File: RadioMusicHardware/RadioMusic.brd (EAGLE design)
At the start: 106 x 49 mm, 63 parts, among them IC2 7805L, IC3 TL072P, IC4 TL072P

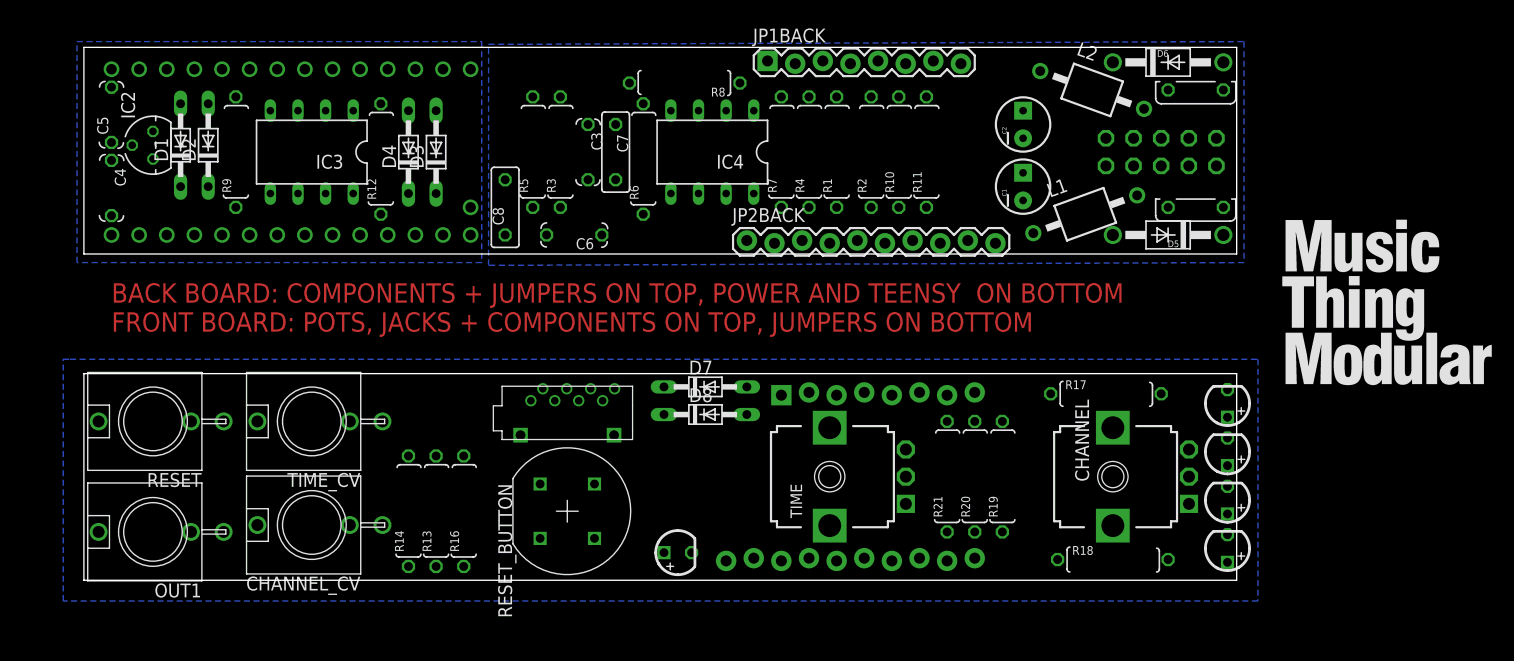
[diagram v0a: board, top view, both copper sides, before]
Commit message: First autorouted board
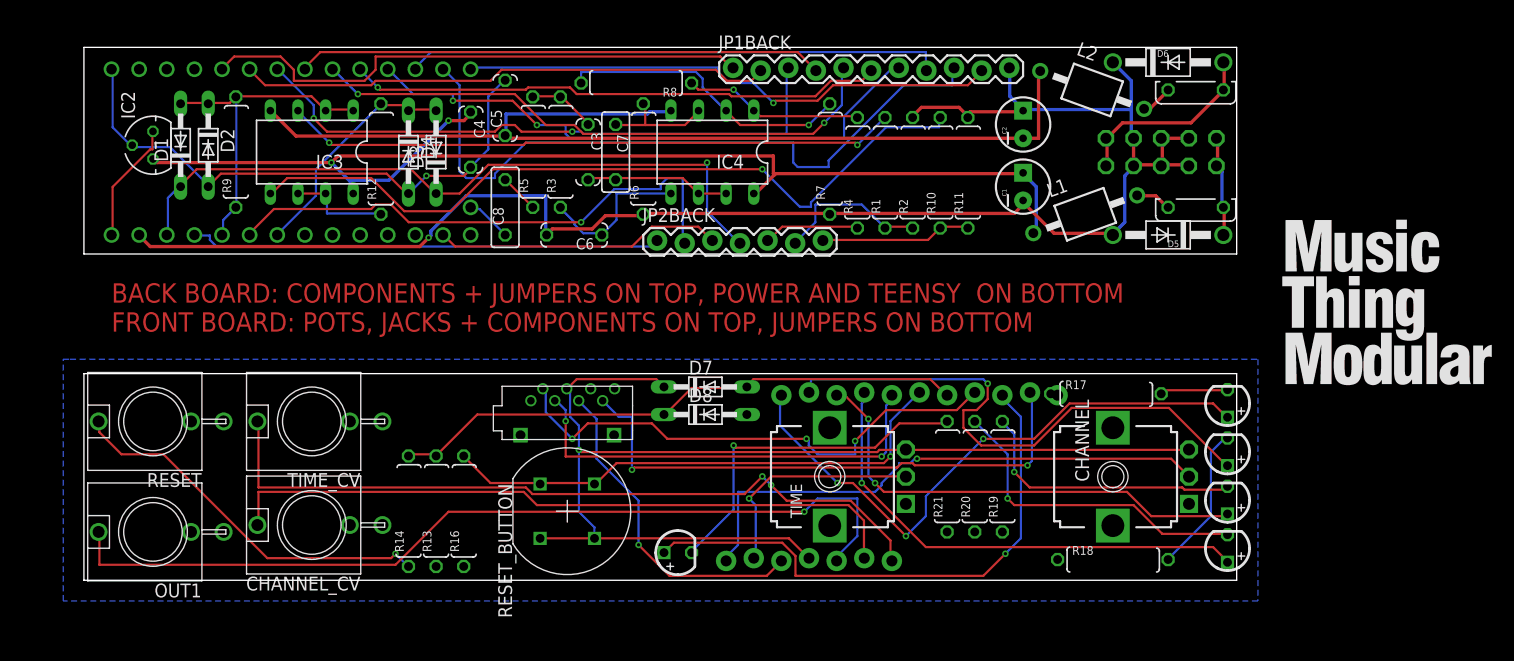
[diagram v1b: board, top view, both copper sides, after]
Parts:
- JP1BACK, JP1FRONT: value (none) -> M11LOCK; device SparkFun-Connectors:1X08_LOCK -> SparkFun-Connectors:1X11_LOCK
- JP2BACK, JP2FRONT: value M10LOCK -> (none); device SparkFun-Connectors:1X10_LOCK -> SparkFun-Connectors:1X07_LOCK
- moved C5 36.2 mm to (38.7, 43.4)
- moved C4 33.3 mm to (35.6, 40.5)
- moved JP2BACK 8.26 mm to (52.7, 31.1)
- moved R4 4.84 mm to (71.1, 37.5)
- moved R1 4.84 mm to (73.7, 37.5)
- moved R7 4.49 mm to (68.6, 38.7)
- moved R8 4.45 mm to (50.8, 45.7)
- moved R11 4.26 mm to (81.3, 37.5)
- moved R2 4.26 mm to (76.2, 37.5)
- moved R10 4.26 mm to (78.7, 37.5)
- moved JP1BACK 3.24 mm to (59.7, 47.0)
- turned D2 to 270 degrees
- turned D4 to 270 degrees
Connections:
- net +3.3V: now also JP2BACK.4; no longer JP2BACK.1
- net +3.3V_F: now also JP2FRONT.4; no longer JP2FRONT.1
- net CHANNEL_CV: now also JP2BACK.6; no longer JP2BACK.8
- net CHANNEL_CV_F: now also JP2FRONT.6; no longer JP2FRONT.8
- net CHANNEL_POT: now also JP2BACK.1; no longer JP2BACK.7
- net CHANNEL_POT_F: now also JP2FRONT.1; no longer JP2FRONT.7
- net GND: now also JP1BACK.11; no longer JP1BACK.8
- net GND_F: now also JP1FRONT.11; no longer JP1FRONT.8
- net LED1: now also JP1BACK.1; no longer JP1BACK.6
- net LED1_F: now also JP1FRONT.1; no longer JP1FRONT.6
- net LED2: now also JP1BACK.2; no longer JP1BACK.5
- net LED2_F: now also JP1FRONT.2; no longer JP1FRONT.5
- net LED3: now also JP1BACK.3; no longer JP1BACK.4
- net LED3_F: now also JP1FRONT.3; no longer JP1FRONT.4
- net LED4: now also JP1BACK.4; no longer JP1BACK.3
- net LED4_F: now also JP1FRONT.4; no longer JP1FRONT.3
- net LED_RESET: now also JP1BACK.9; no longer JP1BACK.2
- net LED_RESET_F: now also JP1FRONT.9; no longer JP1FRONT.2
- net MISO: now also JP1BACK.10; no longer JP2BACK.4
- net MISO_F: now also JP1FRONT.10; no longer JP2FRONT.4
- net MOSI: now also JP1BACK.5; no longer JP2BACK.3
- net MOSI_F: now also JP1FRONT.5; no longer JP2FRONT.3
- net RESET_CV: now also JP1BACK.7; no longer JP2BACK.10
- net RESET_CV_F: now also JP1FRONT.7; no longer JP2FRONT.10
- net RESET_SW: now also JP1BACK.6; no longer JP1BACK.1
- net RESET_SW_F: now also JP1FRONT.6; no longer JP1FRONT.1
- net SCLK: now also JP2BACK.3; no longer JP2BACK.2
- net SCLK_F: now also JP2FRONT.3; no longer JP2FRONT.2
- net SS: now also JP1BACK.8; no longer JP1BACK.7
- net SS_F: now also JP1FRONT.8; no longer JP1FRONT.7
- net TIME_CV: now also JP2BACK.7; no longer JP2BACK.9
- net TIME_CV_F: now also JP2FRONT.7; no longer JP2FRONT.9
- net TIME_POT: now also JP2BACK.2; no longer JP2BACK.6
- net TIME_POT_F: now also JP2FRONT.2; no longer JP2FRONT.6
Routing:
- net GND: track 0.00 -> 152.5 mm, vias 0 -> 1
- net +12V: track 0.00 -> 108.5 mm, vias 0 -> 2
- net +3.3V_F: track 0.00 -> 106.2 mm, vias 0 -> 1
- net -12V: track 0.00 -> 95.3 mm
- net AUDIO_OUT_F: track 0.00 -> 81.8 mm, vias 0 -> 1
- net N$12: track 0.00 -> 70.6 mm, vias 0 -> 1
- net TIME_CV_F: track 0.00 -> 69.5 mm, vias 0 -> 2
- net +3.3V: track 0.00 -> 65.0 mm, vias 0 -> 1
- net LED_RESET: track 0.00 -> 64.3 mm
- net CHANNEL_CV_F: track 0.00 -> 63.4 mm
- net LED3: track 0.00 -> 56.6 mm, vias 0 -> 2
- net N$3: track 0.00 -> 56.5 mm, vias 0 -> 2
- net LED1_F: track 0.00 -> 54.8 mm, vias 0 -> 3
- net RESET_CV: track 0.00 -> 54.3 mm, vias 0 -> 2
- net MOSI: track 0.00 -> 53.9 mm, vias 0 -> 2
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- removed copper zone on layer 16, net DGND
- removed copper zone on layer 16, net GND

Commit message: Add output level trim
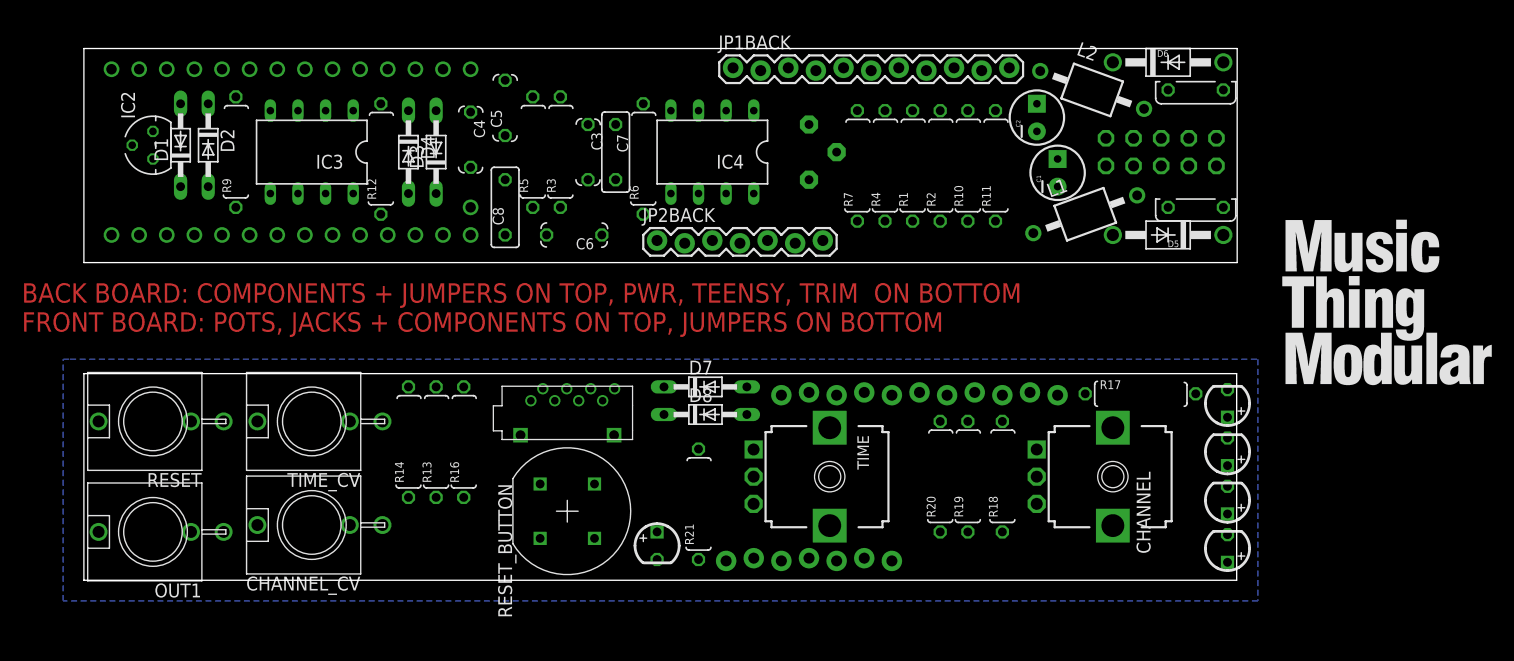
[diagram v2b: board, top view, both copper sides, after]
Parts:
- removed R8: 3.3K, TomW:0207/10
- added R15: (no value), bourns:3362P
- moved R21 23.0 mm to (56.5, 6.99)
- moved R18 12.7 mm to (84.5, 9.53), turned to 90 degrees
- moved R13 6.35 mm to (32.4, 12.7)
- moved R14 6.35 mm to (29.8, 12.7)
- moved R16 6.35 mm to (34.9, 12.7)
- moved C1 3.42 mm to (89.5, 37.5)
- moved R20 3.18 mm to (78.7, 9.53)
- moved R17 3.17 mm to (97.2, 17.1)
- moved R19 3.17 mm to (81.3, 9.53)
- moved R1 2.62 mm to (76.2, 38.1)
- moved R10 2.62 mm to (81.3, 38.1)
- moved R7 2.62 mm to (71.1, 38.1)
- moved R11 2.62 mm to (83.8, 38.1)
- moved R2 2.62 mm to (78.7, 38.1)
- moved R4 2.62 mm to (73.7, 38.1)
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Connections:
- net GND_F: now also R16.2, R20.2, R21.2; no longer R16.1, R20.1, R21.1
- net N$21: now also R20.1; no longer R20.2
- net N$25: now also R21.1; no longer R21.2
- net N$7: now also R15.1; no longer R8.2
- net N$8: now also R15.2, R15.3; no longer R8.1
- net RESET_SW_F: now also R16.1; no longer R16.2
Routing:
- net GND: track 152.5 -> 0.00 mm, vias 1 -> 0
- net +12V: track 108.5 -> 0.00 mm, vias 2 -> 0
- net +3.3V_F: track 106.2 -> 0.00 mm, vias 1 -> 0
- net -12V: track 95.3 -> 0.00 mm
- net AUDIO_OUT_F: track 81.8 -> 0.00 mm, vias 1 -> 0
- net N$12: track 70.6 -> 0.00 mm, vias 1 -> 0
- net TIME_CV_F: track 69.5 -> 0.00 mm, vias 2 -> 0
- net +3.3V: track 65.0 -> 0.00 mm, vias 1 -> 0
- net LED_RESET: track 64.3 -> 0.00 mm
- net CHANNEL_CV_F: track 63.4 -> 0.00 mm
- net LED3: track 56.6 -> 0.00 mm, vias 2 -> 0
- net N$3: track 56.5 -> 0.00 mm, vias 2 -> 0
- net LED1_F: track 54.8 -> 0.00 mm, vias 3 -> 0
- net RESET_CV: track 54.3 -> 0.00 mm, vias 2 -> 0
- net MOSI: track 53.9 -> 0.00 mm, vias 2 -> 0
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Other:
- board size 106 x 49 mm -> 106 x 48.9 mm
- board text added: "BACK BOARD: COMPONENTS + JUMPERS ON TOP, PWR, TEENSY, TRIM ON BOTTOM FRONT BOARD: POTS, JACKS + COMPONENTS ON TOP, JUMPERS ON BOTTOM"
- board text removed: "BACK BOARD: COMPONENTS + JUMPERS ON TOP, POWER AND TEENSY ON BOTTOM FRONT BOARD: POTS, JACKS + COMPONENTS ON TOP, JUMPERS ON BOTTOM"

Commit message: Add reset LED
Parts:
- renumbered R15 to VOLUME

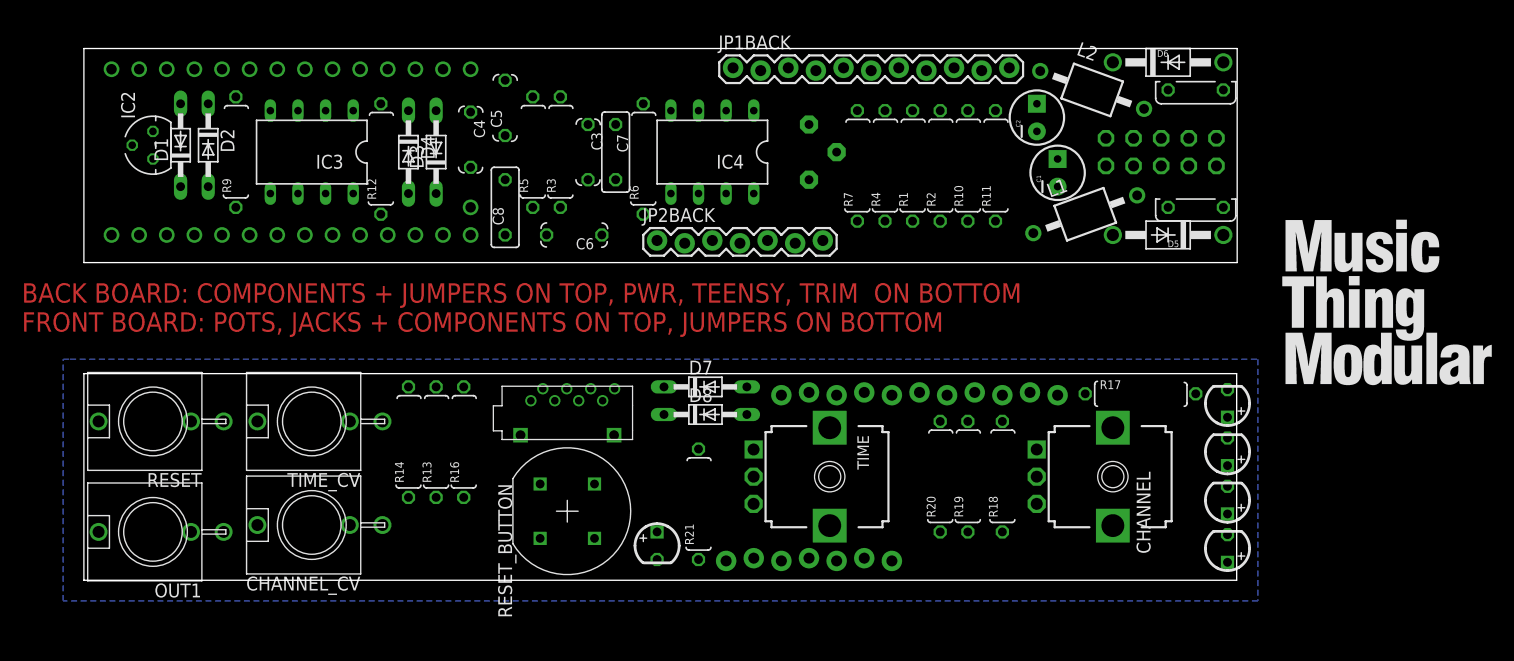
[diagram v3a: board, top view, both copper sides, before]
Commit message: Renumber Parts
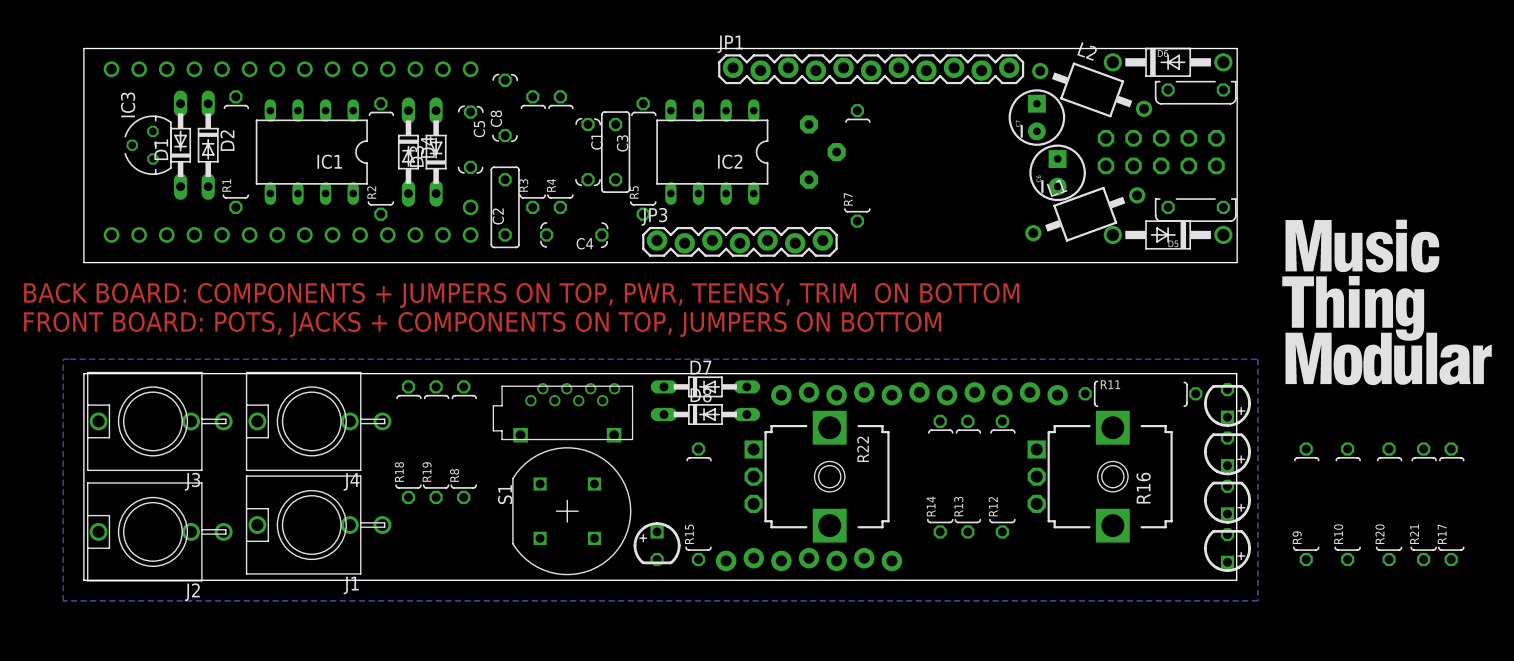
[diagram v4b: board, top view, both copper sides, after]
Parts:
- removed CHANNEL: 50k, TomW:EVUF
- removed IC4: TL072P, TomW:DIL08
- removed VOLUME: (no value), bourns:3362P
- added IC1: TL072P, TomW:DIL08
- added R15: 1k, TomW:0207/10
- added R8: 10k, TomW:0207/10
- C1: value 10uf -> 1n; device SparkFun-Passives:CPOL-RADIAL-10UF-25V -> TomW:C050-024X044
- C2: value 10uf -> 100n; device SparkFun-Passives:CPOL-RADIAL-10UF-25V -> TomW:C050-025X075
- C3: value 1n -> 100n; device TomW:C050-024X044 -> TomW:C050-025X075
- C4: value 100n -> 1n
- C6: value 1n -> 10uf; device TomW:C050-024X044 -> SparkFun-Passives:CPOL-RADIAL-10UF-25V
- C7: value 100n -> 10uf; device TomW:C050-025X075 -> SparkFun-Passives:CPOL-RADIAL-10UF-25V
- C8: device TomW:C050-025X075 -> TomW:C050-024X044
- IC2: value 7805L -> TL072P; device gm-regulators:TO92 -> TomW:DIL08
- IC3: value TL072P -> 7805L; device TomW:DIL08 -> gm-regulators:TO92
- R1: value 100k -> 47R
- R10: value 100k -> 200k
- R11: value 200k -> 1k
- R12: value 47R -> 1k
- R13: value 100k -> 1k
- R14: value 220R -> 1k
- R16: value 10k -> 50k; device TomW:0207/10 -> TomW:EVUF
- R17, R18: value 1k -> 220R
- R19, R20: value 1k -> 100k
- R2: value 200k -> 47R
- R21: value 1k -> 200k
- R4: value 220R -> 8.2k
- R5: value 8.2k -> 330K
- R6: value 330K -> (none); device TomW:0207/10 -> bourns:3362P
- R9: value 47R -> 100k
- moved R9 103.6 mm to (112.4, 6.99)
- moved R21 66.7 mm to (123.2, 6.99)
- moved R12 64.2 mm to (84.5, 9.53)
- moved R1 62.2 mm to (14.0, 39.4)
- moved R16 59.8 mm to (94.6, 9.53), turned to 270 degrees
- moved R18 54.7 mm to (29.8, 12.7)
- moved IC2 51.4 mm to (57.8, 39.4), turned to 180 degrees
- moved R2 51.4 mm to (27.3, 38.7)
- moved C2 49.6 mm to (38.7, 34.3)
- moved R13 49.0 mm to (81.3, 9.53)
- moved R19 49.0 mm to (32.4, 12.7)
- moved R14 49.0 mm to (78.7, 9.53)
- moved R10 46.8 mm to (116.2, 6.99)
- moved C6 44.8 mm to (89.5, 37.5), turned to 90 degrees
- moved C1 43.2 mm to (46.4, 39.4), turned to 270 degrees
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- renumbered 1 to F1, CHANNEL_CV to J1, FUSE to F2, JP1BACK to JP1, JP1FRONT to JP2, JP2BACK to JP3, JP2FRONT to JP4, OUT1 to J2, RESET to J3, RESET_BUTTON to S1, RESET_LED to LED5, TIME to R22, TIME_CV to J4, U$1 to U1, U$3 to X1
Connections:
- removed net N$12: IC3.5, R10.2
- removed net N$8: IC4.1, R4.2, VOLUME.2, VOLUME.3
- new net N$9: J1.P$1, R10.1, R9.1
- new net TEMP: J4.P$1, R20.1, R21.1
- net +12V: now also C5.1, C6.1, IC1.8, IC2.8, IC3.1; no longer C1.1, C4.1, IC2.1, IC3.8, IC4.8
- net +3.3V_F: now also R16.3; no longer CHANNEL.3
- net +5V: now also IC3.3; no longer IC2.3
- net -12V: now also C7.2, C8.1, IC1.4, IC2.4; no longer C2.2, C5.1, IC3.4, IC4.4
- net AUDIO_OUT: now also IC2.1, R6.2, R6.3; no longer R4.1
- net AUDIO_OUT_F: now also R17.2; no longer J2.P$1
- net CHANNEL_CV: now also IC1.3; no longer R1.1, R2.1
- net CHANNEL_CV_F: now also R9.2; no longer J1.P$1
- net CHANNEL_POT_F: now also R16.2; no longer CHANNEL.2
- net DAC: now also C2.1; no longer C8.1
- net DGND: now also C8.2, IC3.2; no longer C4.2, IC2.2
- net GND: now also C4.2, C7.1, R10.2, R21.2, R5.1; no longer C1.2, C2.1, R11.2, R2.2, R6.1
- net GND_F: now also R11.1, R12.1, R14.2, R15.2, R16.1, R8.2; no longer CHANNEL.1, R16.2, R17.1, R18.1, R20.2, R21.2
- net N$1: now also IC1.6, IC1.7, R2.1; no longer IC3.6, IC3.7, R12.1
- net N$10: now also C2.2, R3.1; no longer C8.2, R5.1
- net N$14: now also R18.1; no longer R14.1
- net N$18: now also R11.2; no longer R17.2
- net N$19: now also R12.2; no longer R18.2
- net N$2: now also C4.1, IC2.5, R4.1; no longer C6.1, IC4.5, R3.1
- net N$20: now also R13.2; no longer R19.2
- net N$21: now also R14.1; no longer R20.1
- net N$25: now also R15.1; no longer R21.1
- net N$3: now also J2.P$1, R17.1; no longer IC3.3, R1.2
- net N$4: now also C1.1, R4.2; no longer C3.1, R5.2
- net N$5: now also C1.2, IC2.6, IC2.7; no longer C7.2, IC4.6, IC4.7
- net N$6: now also C3.1, IC2.3, R5.2; no longer C7.1, IC4.3, R6.2
- net N$7: now also IC2.2, R6.1; no longer IC4.2, VOLUME.1
- net PIN20/A6: now also R2.2; no longer R12.2
- net PIN22/A8: now also IC1.1, IC1.2, R1.1, R1.2; no longer IC3.1, IC3.2, R9.1, R9.2
- net RESET_CV_F: now also R18.2, R19.2; no longer R13.2, R14.2
- net RESET_SW_F: now also R8.1; no longer R16.1
- net TIME_CV: now also IC1.5; no longer R10.1, R11.1
- net TIME_CV_F: now also R20.2; no longer J4.P$1
